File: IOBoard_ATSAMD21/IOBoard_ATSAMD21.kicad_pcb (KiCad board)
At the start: 2 copper layers, 76.2 x 128.5 mm, 36 parts, among them J1 Conn_PIC_ICSP_ICD, J2 Conn_01x04_Male, SW1 EG_1218, SW2 EG_1218, SW3 EG_1218, SW4 EG_1218, U1 ATSAMD21G18A-A, U2 AP2112K-3.3

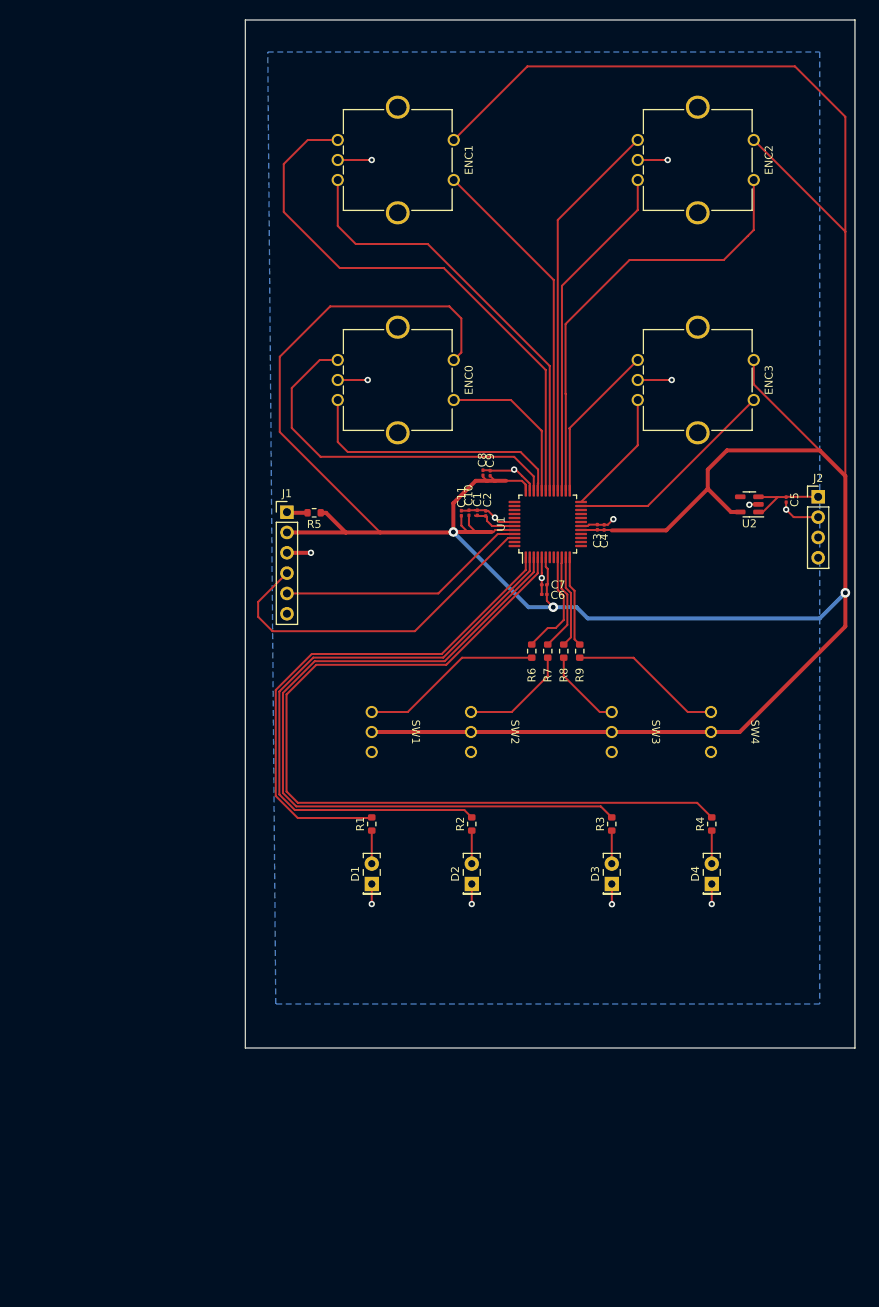
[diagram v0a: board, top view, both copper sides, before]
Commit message: IO Board Silkscreening Finished
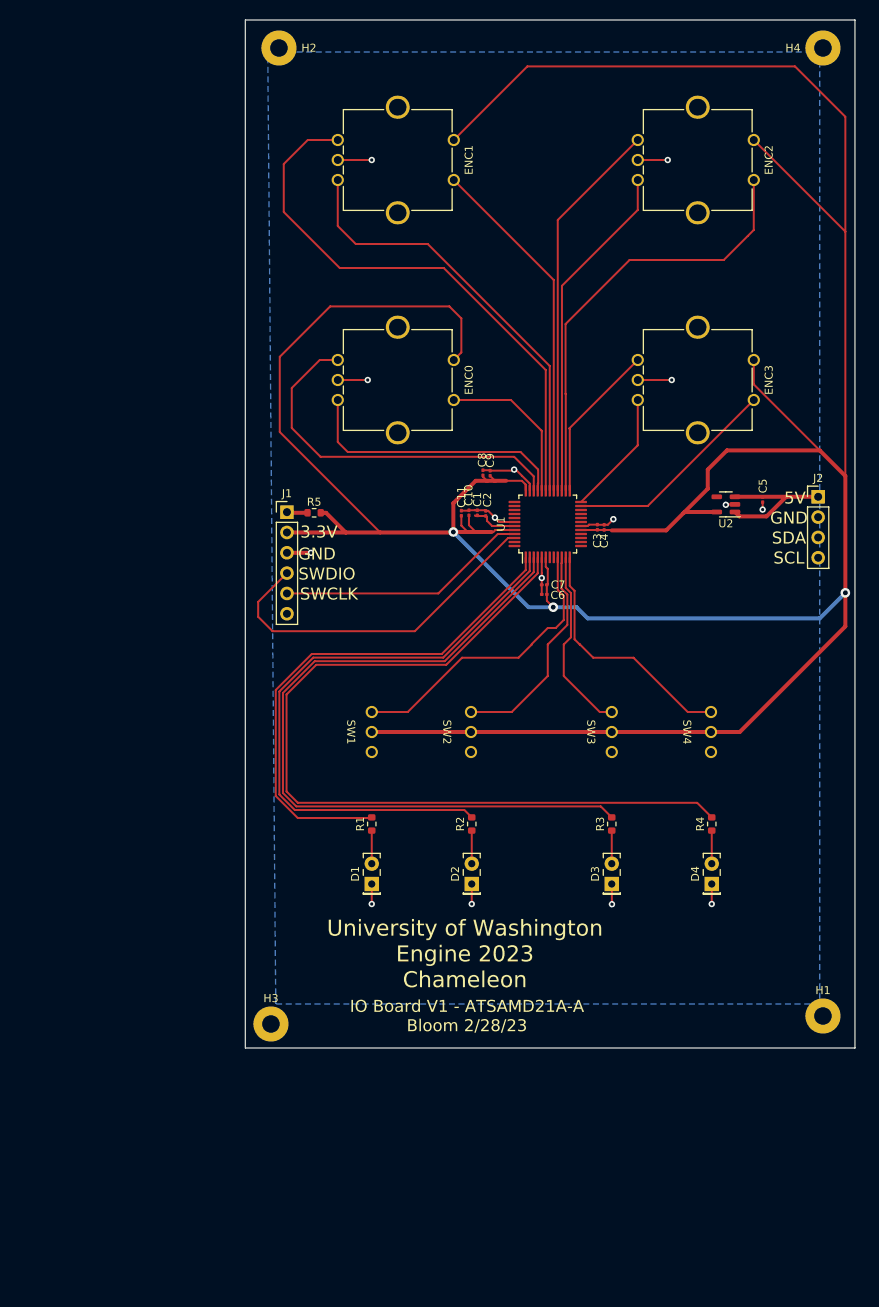
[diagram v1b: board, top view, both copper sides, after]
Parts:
- removed R6, R7, R8, R9: 10k, Resistor_SMD:R_0603_1608Metric
- added H1: MountingHole_Pad, MountingHole:MountingHole_2.2mm_M2_Pad, F.Cu at (138.0, 166.0)
- added H2: MountingHole_Pad, MountingHole:MountingHole_2.2mm_M2_Pad, F.Cu at (70.0, 45.0)
- added H3: MountingHole_Pad, MountingHole:MountingHole_2.2mm_M2_Pad, F.Cu at (69.0, 167.0)
- added H4: MountingHole_Pad, MountingHole:MountingHole_2.2mm_M2_Pad, F.Cu at (138.0, 45.0)
- moved U2 2.94 mm to (125.9, 102.0)
- moved C5 2.94 mm to (130.5, 101.5)
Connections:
- SW1 pad 2: Net-(SW1-Pad2) -> /SW0
- SW2 pad 2: Net-(SW2-Pad2) -> /SW1
- SW3 pad 2: Net-(SW3-Pad2) -> /SW2
- SW4 pad 2: Net-(SW4-Pad2) -> /SW3
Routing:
- net /SW0: track 13.5 -> 36.9 mm
- net Net-(SW1-Pad2): track 22.8 -> 0.00 mm
- net /SW3: track 11.4 -> 31.3 mm
- net Net-(SW4-Pad2): track 19.2 -> 0.00 mm
- net /SW1: track 11.5 -> 26.9 mm
- net Net-(SW2-Pad2): track 13.7 -> 0.00 mm
- net /SW2: track 11.5 -> 23.3 mm
- net Net-(SW3-Pad2): track 10.1 -> 0.00 mm
- net VCC: track 10.7 -> 18.7 mm
- net GND: track 59.7 -> 55.3 mm
- net +3.3V: track 434.1 -> 433.0 mm
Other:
- board text added: "3.3V"
- board text added: "5V"
- board text added: "GND"
- board text added: "IO Board V1 - ATSAMD21A-A Bloom 2/28/23"
- board text added: "SCL"
- board text added: "SDA"
- board text added: "SWCLK"
- board text added: "SWDIO"
- board text added: "University of Washington Engine 2023 Chameleon"

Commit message: updating lab PC
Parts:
- C1, C10, C11, C2, C3, C4, C5, C6, C7, C8, C9: footprint Capacitor_SMD:C_0201_0603Metric -> Capacitor_SMD:C_0603_1608Metric
- ENC0, ENC1, ENC2, ENC3: footprint Rotary_Encoder:RotaryEncoder_Bourns_Vertical_PEC12R-3xxxF-Sxxxx -> custom_lib:PEC12R-3217F-S0024-ND
- moved ENC3 16.1 mm to (124.2, 97.1)
- moved ENC1 16.0 mm to (87.2, 69.1)
- moved ENC0 15.7 mm to (86.8, 96.6)
- moved ENC2 15.7 mm to (124.2, 69.1)
- moved C11 5.34 mm to (87.5, 102.5)
- moved C3 5.08 mm to (114.8, 106.0), turned to -90 degrees
- moved C10 3.85 mm to (90.0, 102.5)
- moved C8 3.03 mm to (98.5, 98.5)
- moved C4 2.60 mm to (113.0, 106.0), turned to 90 degrees
- moved C1 2.14 mm to (92.8, 102.5)
- moved C5 1.71 mm to (129.2, 100.2), turned to 90 degrees
- moved C6 1.22 mm to (103.0, 114.5)
- moved C2 1.10 mm to (95.0, 102.5)
- moved C7 0.68 mm to (103.0, 112.8)
- moved C9 0.36 mm to (96.5, 98.5)
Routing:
- net /SDA: track 0.00 -> 41.6 mm
- net /SCL: track 0.00 -> 30.9 mm
- net GND: track 55.3 -> 48.6 mm, vias 15 -> 11
- net +3.3V: track 433.0 -> 438.6 mm
- net Net-(C1-Pad2): track 5.75 -> 7.31 mm
- removed copper zone on B.Cu, net GND

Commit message: adc v5
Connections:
- SW1 pad 1: +3.3V -> GND
- SW2 pad 1: +3.3V -> GND
- SW3 pad 1: +3.3V -> GND
- SW4 pad 1: +3.3V -> GND
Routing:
- net +3.3V: track 438.6 -> 375.8 mm
- net GND: track 48.6 -> 48.4 mm, vias 11 -> 12
- added copper zone on B.Cu, net GND
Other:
- board text added: "IO Board V1.1 - ATSAMD21A-A Bloom 3/8/23"
- board text removed: "IO Board V1 - ATSAMD21A-A Bloom 2/28/23"
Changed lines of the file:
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@@
     (fp_rect (start 5.8 3) (end -5.8 7) (layer "F.CrtYd") (width 0.05) (fill none))
     (pad "1" thru_hole circle (at 0 5 270) (size 1.524 1.524) (drill 1) (layers *.Cu *.Mask)
-      (net 3 "+3.3V") (pintype "passive") (zone_connect 2))
+      (net 1 "GND") (pintype "passive") (zone_connect 2))
     (pad "2" thru_hole circle (at -2.5 5 270) (size 1.524 1.524) (drill 1) (layers *.Cu *.Mask)
       (net 21 "/SW2") (pintype "passive") (zone_connect 2))
@@
     (fp_rect (start 5.8 3) (end -5.8 7) (layer "F.CrtYd") (width 0.05) (fill none))
     (pad "1" thru_hole circle (at 0 5 270) (size 1.524 1.524) (drill 1) (layers *.Cu *.Mask)
-      (net 3 "+3.3V") (pintype "passive") (zone_connect 2))
+      (net 1 "GND") (pintype "passive") (zone_connect 2))
     (pad "2" thru_hole circle (at -2.5 5 270) (size 1.524 1.524) (drill 1) (layers *.Cu *.Mask)
       (net 17 "/SW0") (pintype "passive") (zone_connect 2))
@@
     (fp_rect (start -5.8 3) (end 5.8 7) (layer "F.CrtYd") (width 0.05) (fill none))
     (pad "1" thru_hole circle (at 0 5 270) (size 1.524 1.524) (drill 1) (layers *.Cu *.Mask)
-      (net 3 "+3.3V") (pintype "passive") (zone_connect 2))
+      (net 1 "GND") (pintype "passive") (zone_connect 2))
     (pad "2" thru_hole circle (at -2.5 5 270) (size 1.524 1.524) (drill 1) (layers *.Cu *.Mask)
       (net 23 "/SW3") (pintype "passive") (zone_connect 2))
@@
     (fp_rect (start 5.8 3) (end -5.8 7) (layer "F.CrtYd") (width 0.05) (fill none))
     (pad "1" thru_hole circle (at 0 5 270) (size 1.524 1.524) (drill 1) (layers *.Cu *.Mask)
-      (net 3 "+3.3V") (pintype "passive") (zone_connect 2))
+      (net 1 "GND") (pintype "passive") (zone_connect 2))
     (pad "2" thru_hole circle (at -2.5 5 270) (size 1.524 1.524) (drill 1) (layers *.Cu *.Mask)
       (net 19 "/SW1") (pintype "passive") (zone_connect 2))
@@
     (effects (font (size 1.5 1.5) (thickness 0.3)))
   )
-  (gr_text "IO Board V1 - ATSAMD21A-A\nBloom 2/28/23" (at 93.5 166) (layer "F.SilkS")
+  (gr_text "IO Board V1.1 - ATSAMD21A-A\nBloom 3/8/23" (at 93.5 166) (layer "F.SilkS")
     (effects (font (size 1.5 1.5) (thickness 0.3)))
   )
@@
   )
   (segment (start 102.2 112.75) (end 102.2 114.5) (width 0.25) (layer "F.Cu") (net 1))
-  (segment (start 99.265 97.835) (end 99.4 97.7) (width 0.25) (layer "F.Cu") (net 1))
   (segment (start 109.75 104.75) (end 110.595019 103.985251) (width 0.25) (layer "F.Cu") (net 1))
-  (segment (start 89.975 101.7) (end 92.75 101.7) (width 0.25) (layer "F.Cu") (net 1))
+  (segment (start 89.975 101.7) (end 91.3 101.7) (width 0.25) (layer "F.Cu") (net 1))
   (segment (start 113 106.8) (end 114.75 106.8) (width 0.25) (layer "F.Cu") (net 1))
   (segment (start 89.95 101.725) (end 89.975 101.7) (width 0.25) (layer "F.Cu") (net 1))
-  (segment (start 100.4 98.5) (end 99.6 97.7) (width 0.25) (layer "F.Cu") (net 1))
+  (segment (start 100.4 98.5) (end 99.95 98.05) (width 0.25) (layer "F.Cu") (net 1))
   (segment (start 102.2 111.55) (end 102.2 112.75) (width 0.25) (layer "F.Cu") (net 1))
   (segment (start 114.75 106.8) (end 115.3 106.8) (width 0.25) (layer "F.Cu") (net 1))
@@
   (segment (start 89.925 101.7) (end 89.95 101.725) (width 0.25) (layer "F.Cu") (net 1))
   (segment (start 102.2 114.5) (end 102.2 114.55) (width 0.25) (layer "F.Cu") (net 1))
+  (segment (start 99.95 98.05) (end 99.6 97.7) (width 0.25) (layer "F.Cu") (net 1))
   (segment (start 99.6 97.7) (end 99.4 97.7) (width 0.25) (layer "F.Cu") (net 1))
   (segment (start 111.622618 152.02836) (end 111.6 152) (width 0.25) (layer "F.Cu") (net 1))
@@
   (segment (start 102.85 108.6625) (end 102.85 110.9) (width 0.25) (layer "F.Cu") (net 1))
   (segment (start 94.1 149.5) (end 94.1 152) (width 0.25) (layer "F.Cu") (net 1))
+  (segment (start 91.3 101.7) (end 92.75 101.7) (width 0.25) (layer "F.Cu") (net 1))
   (segment (start 96.525 97.75) (end 96.5 97.725) (width 0.25) (layer "F.Cu") (net 1))
   (segment (start 99.4375 104.25) (end 97.55 104.25) (width 0.25) (layer "F.Cu") (net 1))
@@
   (via (at 110.595019 103.985251) (size 0.8) (drill 0.4) (layers "F.Cu" "B.Cu") (net 1))
   (via (at 125.8625 102.1) (size 0.8) (drill 0.4) (layers "F.Cu" "B.Cu") (net 1))
-  (via (at 99.4 97.7) (size 0.8) (drill 0.4) (layers "F.Cu" "B.Cu") (net 1))
   (via (at 100.25 116.5) (size 0.8) (drill 0.4) (layers "F.Cu" "B.Cu") (net 1))
   (via (at 116.75 108.25) (size 0.8) (drill 0.4) (layers "F.Cu" "B.Cu") (net 1))
+  (via (at 99.95 98.05) (size 0.8) (drill 0.4) (layers "F.Cu" "B.Cu") (net 1))
+  (via (at 91.3 101.7) (size 0.8) (drill 0.4) (layers "F.Cu" "B.Cu") (net 1))
   (via (at 124.1 152) (size 0.8) (drill 0.4) (layers "F.Cu" "B.Cu") (net 1))
   (via (at 97 103.7) (size 0.8) (drill 0.4) (layers "F.Cu" "B.Cu") (net 1))
@@
   (segment (start 123.6 100.1) (end 123.6 97.7) (width 0.5) (layer "F.Cu") (net 3))
   (segment (start 91.8 105.5) (end 93.6 105.5) (width 0.5) (layer "F.Cu") (net 3))
-  (segment (start 100.85 99.586396) (end 100.363604 99.1) (width 0.25) (layer "F.Cu") (net 3))
   (segment (start 70.1 93) (end 70.1 83.6) (width 0.5) (layer "F.Cu") (net 3))
   (segment (start 87.525 103.275) (end 87.5 103.25) (width 0.25) (layer "F.Cu") (net 3))
@@
   (segment (start 89.95 103.275) (end 87.525 103.275) (width 0.25) (layer "F.Cu") (net 3))
   (segment (start 78.34 105.56) (end 71 105.56) (width 0.5) (layer "F.Cu") (net 3))
-  (segment (start 98.5 99.3) (end 100.163604 99.3) (width 0.25) (layer "F.Cu") (net 3))
   (segment (start 103.75 112.75) (end 103.75 114.5) (width 0.5) (layer "F.Cu") (net 3))
   (segment (start 94.6 105.5) (end 96.6 105.5) (width 0.5) (layer "F.Cu") (net 3))
   (segment (start 70.1 83.6) (end 76.4 77.3) (width 0.5) (layer "F.Cu") (net 3))
-  (segment (start 100.163604 99.3) (end 100.363604 99.1) (width 0.25) (layer "F.Cu") (net 3))
   (segment (start 129.35 84) (end 129.35 87.05) (width 0.5) (layer "F.Cu") (net 3))
   (segment (start 75.225 103.1) (end 75.88 103.1) (width 0.5) (layer "F.Cu") (net 3))
@@
   (segment (start 82.66 105.56) (end 76.425 99.325) (width 0.5) (layer "F.Cu") (net 3))
   (segment (start 111.55 105.25) (end 107.7625 105.25) (width 0.25) (layer "F.Cu") (net 3))
+  (segment (start 99.8125 99.3) (end 98.5 99.3) (width 0.25) (layer "F.Cu") (net 3))
   (segment (start 76.425 99.325) (end 70.1 93) (width 0.5) (layer "F.Cu") (net 3))
   (segment (start 76.475 99.275) (end 76.425 99.325) (width 0.5) (layer "F.Cu") (net 3))
@@
   (segment (start 124.725 103) (end 120.7 103) (width 0.5) (layer "F.Cu") (net 3))
   (segment (start 96.5 99.275) (end 98.475 99.275) (width 0.25) (layer "F.Cu") (net 3))
-  (segment (start 100.85 100.3375) (end 100.85 99.586396) (width 0.25) (layer "F.Cu") (net 3))
   (segment (start 103.75 112.75) (end 103.75 110.25) (width 0.5) (layer "F.Cu") (net 3))
   (segment (start 93.6 105.5) (end 94.6 105.5) (width 0.5) (layer "F.Cu") (net 3))
@@
   (segment (start 89.56 105.56) (end 82.66 105.56) (width 0.5) (layer "F.Cu") (net 3))
   (segment (start 140.8 98.5) (end 140.8 113.1) (width 0.5) (layer "F.Cu") (net 3))
+  (segment (start 100.85 100.3375) (end 99.8125 99.3) (width 0.25) (layer "F.Cu") (net 3))
   (segment (start 126 95.3) (end 137.6 95.3) (width 0.5) (layer "F.Cu") (net 3))
   (segment (start 129.35 87.05) (end 137.6 95.3) (width 0.5) (layer "F.Cu") (net 3))
@@
   (via (at 91.8 105.5) (size 1.2) (drill 0.6) (layers "F.Cu" "B.Cu") (net 3))
   (via (at 140.8 113.1) (size 1.2) (drill 0.6) (layers "F.Cu" "B.Cu") (net 3))
-  (segment (start 111.6 130.5) (end 94.005 130.5) (width 0.5) (layer "B.Cu") (net 3))
   (segment (start 91.8 105.5) (end 101.2 114.9) (width 0.5) (layer "B.Cu") (net 3))
   (segment (start 101.2 114.9) (end 104.285 114.9) (width 0.5) (layer "B.Cu") (net 3))
   (segment (start 137.6 116.3) (end 108.6 116.3) (width 0.5) (layer "B.Cu") (net 3))
   (segment (start 103.75 116) (end 104.85 114.9) (width 0.5) (layer "B.Cu") (net 3))
-  (segment (start 94.005 130.5) (end 81.6 130.5) (width 0.5) (layer "B.Cu") (net 3))
   (segment (start 104.85 114.9) (end 105.15 114.9) (width 0.5) (layer "B.Cu") (net 3))
   (segment (start 140.8 113.1) (end 137.6 116.3) (width 0.5) (layer "B.Cu") (net 3))
-  (segment (start 137.6 116.3) (end 137.6 116.905) (width 0.5) (layer "B.Cu") (net 3))
   (segment (start 107.2 114.9) (end 108.6 116.3) (width 0.5) (layer "B.Cu") (net 3))
   (segment (start 105.15 114.9) (end 107.2 114.9) (width 0.5) (layer "B.Cu") (net 3))
   (segment (start 104.285 114.9) (end 105.15 114.9) (width 0.5) (layer "B.Cu") (net 3))
-  (segment (start 137.6 116.905) (end 124.005 130.5) (width 0.5) (layer "B.Cu") (net 3))
-  (segment (start 124.005 130.5) (end 111.6 130.5) (width 0.5) (layer "B.Cu") (net 3))
   (segment (start 127.035 101.135) (end 127 101.1) (width 0.25) (layer "F.Cu") (net 4))
   (segment (start 127.5625 103) (end 127 103) (width 0.25) (layer "F.Cu") (net 4))
@@
   (segment (start 107.7625 106.75) (end 110 106.75) (width 0.25) (layer "F.Cu") (net 40))
   (segment (start 112.5 109.25) (end 136.87 109.25) (width 0.25) (layer "F.Cu") (net 40))
+  (zone (net 1) (net_name "GND") (layer "B.Cu") (hatch edge 0.508)
+    (connect_pads (clearance 0.508))
+    (min_thickness 0.254) (filled_areas_thickness no)
+    (fill yes (thermal_gap 0.508) (thermal_bridge_width 0.508))
+    (polygon
+      (pts
+        (xy 143 173)
+        (xy 65 173)
+        (xy 65 41)
+        (xy 143 41)
+      )
+    )
+  )
 )

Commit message: IOBoard V2 + documentation
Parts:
- H1, H2, H3, H4: footprint MountingHole:MountingHole_2.2mm_M2_Pad -> MountingHole:MountingHole_3.2mm_M3_ISO7380_Pad
- SW1, SW2, SW3, SW4: footprint Custom:EG_1218 -> custom_lib:EG_1218
- moved H1 138.8 mm to (57.5, 53.0)
- moved H4 132.0 mm to (118.4, 175.5)
- moved H2 49.1 mm to (118.4, 53.0)
- moved R1 29.7 mm to (65.2, 166.8)
- moved R3 29.5 mm to (95.7, 166.8)
- moved R2 28.3 mm to (80.5, 166.8)
- moved R4 28.1 mm to (111.0, 166.8)
- moved SW3 23.6 mm to (95.7, 141.4)
- moved U2 22.4 mm to (108.4, 116.0)
- moved J2 21.9 mm to (121.4, 116.0)
- moved SW2 21.5 mm to (80.5, 141.4)
- moved C5 21.1 mm to (116.1, 116.8), turned to -90 degrees
- moved SW4 21.1 mm to (111.0, 141.4)
- moved D1 20.5 mm to (65.2, 161.9)
- moved D3 20.1 mm to (95.7, 161.8)
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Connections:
- D1 pad 1: GND -> Net-(D1-Pad1)
- D1 pad 2: Net-(D1-Pad2) -> /LED0
- D2 pad 1: GND -> Net-(D2-Pad1)
- D2 pad 2: Net-(D2-Pad2) -> /LED1
- D3 pad 1: GND -> Net-(D3-Pad1)
- D3 pad 2: Net-(D3-Pad2) -> /LED2
- D4 pad 1: GND -> Net-(D4-Pad1)
- D4 pad 2: Net-(D4-Pad2) -> /LED3
- J2 pad 3: /SDA -> /SCL
- J2 pad 4: /SCL -> /SDA
- R1 pad 1: Net-(D1-Pad2) -> GND
- R1 pad 2: /LED0 -> Net-(D1-Pad1)
- R2 pad 1: Net-(D2-Pad2) -> GND
- R2 pad 2: /LED1 -> Net-(D2-Pad1)
- R3 pad 1: Net-(D3-Pad2) -> GND
- R3 pad 2: /LED2 -> Net-(D3-Pad1)
- R4 pad 1: Net-(D4-Pad2) -> GND
- R4 pad 2: /LED3 -> Net-(D4-Pad1)
- SW1 pad 1: GND -> +3.3V
- SW2 pad 1: GND -> +3.3V
- SW3 pad 1: GND -> +3.3V
- SW4 pad 1: GND -> +3.3V
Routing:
- net +3.3V: track 375.8 -> 13.9 mm, vias 3 -> 0
- net /ENC1_SW: track 44.0 -> 80.7 mm
- net /ENC0_SW: track 21.4 -> 55.9 mm
- net /ENC0_A: track 46.7 -> 22.3 mm
- net /ENC1_A: track 70.0 -> 48.3 mm
- net /SDA: track 41.6 -> 31.2 mm
- net /ENC3_B: track 15.7 -> 25.4 mm
- net /ENC0_B: track 34.5 -> 27.5 mm
- net /ENC3_A: track 19.9 -> 26.9 mm
- net /ENC3_SW: track 27.1 -> 32.5 mm
- net GND: track 48.4 -> 43.2 mm, vias 12 -> 10
- net /ENC2_SW: track 55.5 -> 60.6 mm
- net /ENC2_B: track 42.8 -> 47.7 mm
- net /ENC2_A: track 48.0 -> 52.9 mm
- net /LED0: track 65.5 -> 70.2 mm
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- added copper zone on F.Cu, net +3.3V
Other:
- board text added: "IO Board - ATSAMD21G18AU V2 Bloom 3/30/23"
- board text added: "MCLR"
- board text added: "NC"
- board text added: "University of Washington Engine 2023 - Chameleon"
- board text added: "VCC"
- board text removed: "3.3V"
- board text removed: "5V"
- board text removed: "IO Board V1.1 - ATSAMD21A-A Bloom 3/8/23"
- board text removed: "IOBoard ATSAMD21 V1"
- board text removed: "University of Washington Engine 2023 Chameleon"
